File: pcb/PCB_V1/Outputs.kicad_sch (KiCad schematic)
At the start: 18 parts, among them J501 FAN1 / WAGO 2601, J511 FAN2 / WAGO 2601, J521 PUMP + / switched -, Q501 AO3400A, Q511 AO3400A, Q521 AO3400A

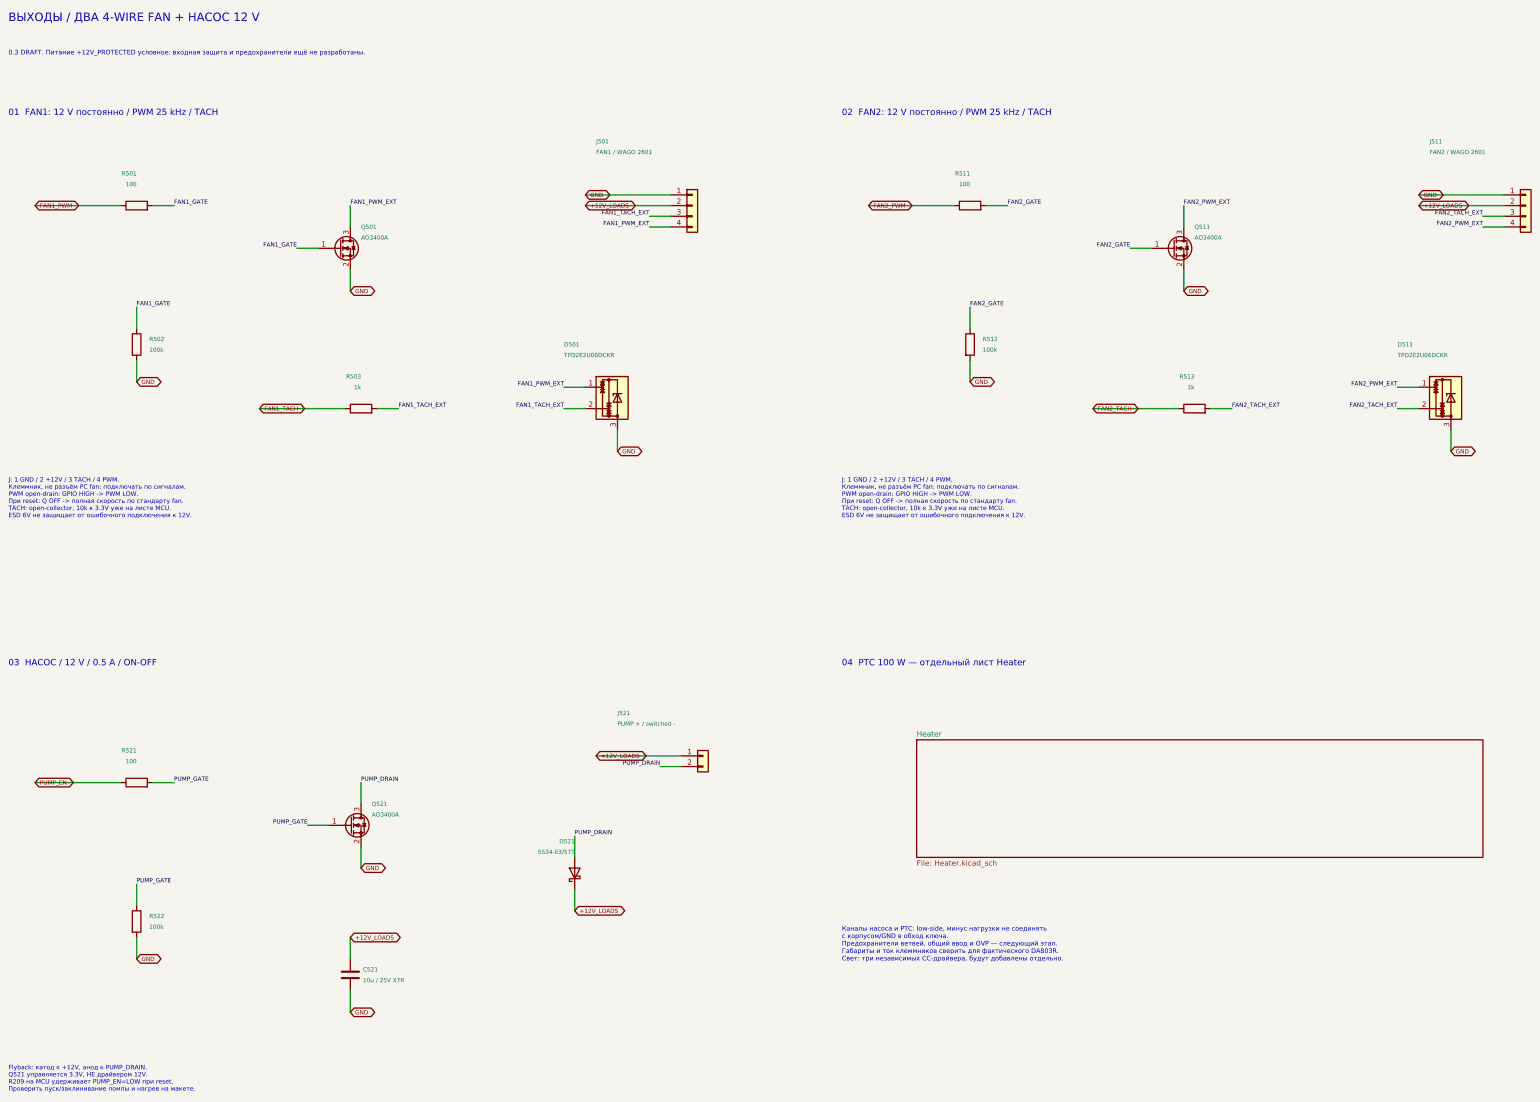
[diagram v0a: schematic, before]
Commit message: pcb: move board to 24 V input with 12 V aux buck and merged LED bar channel
Revision 0.14 of PCB_V1 (see pcb/PCB_V1/REDESIGN_24V.md):
- 24 V input on keyed XT60PW-M (pin 1 GND, pin 2 +24V); LM74700, input
  MOSFET and F901 removed; SMBJ26CA TVS; 220 uF/50 V bulk
- ATM mini-blade fuses in XF-508P-B-B holders: F902 10 A loads, F903 7.5 A LED
- new LMR16020 24 V -> 12 V aux buck (500 kHz) feeding PC fans, the
  UCC27524A heater gate driver and the TPS54202 3.3 V buck; TPS70950 removed
- heater and pump on 24 V: SMBJ30A drain TVS, AO3422 + SS36 pump stage
- LED CH1 panel keeps SRP1770TA/0.027 R/1k, switch now CSD19534Q5A;
  CH2 drives both identical bars in parallel (J721 || J731, 0.40 R);
  third AL8853 channel removed
- TS-1187A buttons, DORABO/KANGNEX terminals
- project library: LMR16020 and CSD19534Q5A symbols, TI DQJ and XF-508P
  footprints
- verify_netlist.py / verify_board.py / analyze_*.py updated for 24 V;
  new sync_board.py updates the unrouted staging board from the netlist
- ERC 0/0; netlist, board and sizing checks pass; DRC only the 12 known
  ESP32 drill sizes plus unrouted connections; 163 components

Co-Authored-By: Claude Opus 5.5 <noreply@anthropic.com>
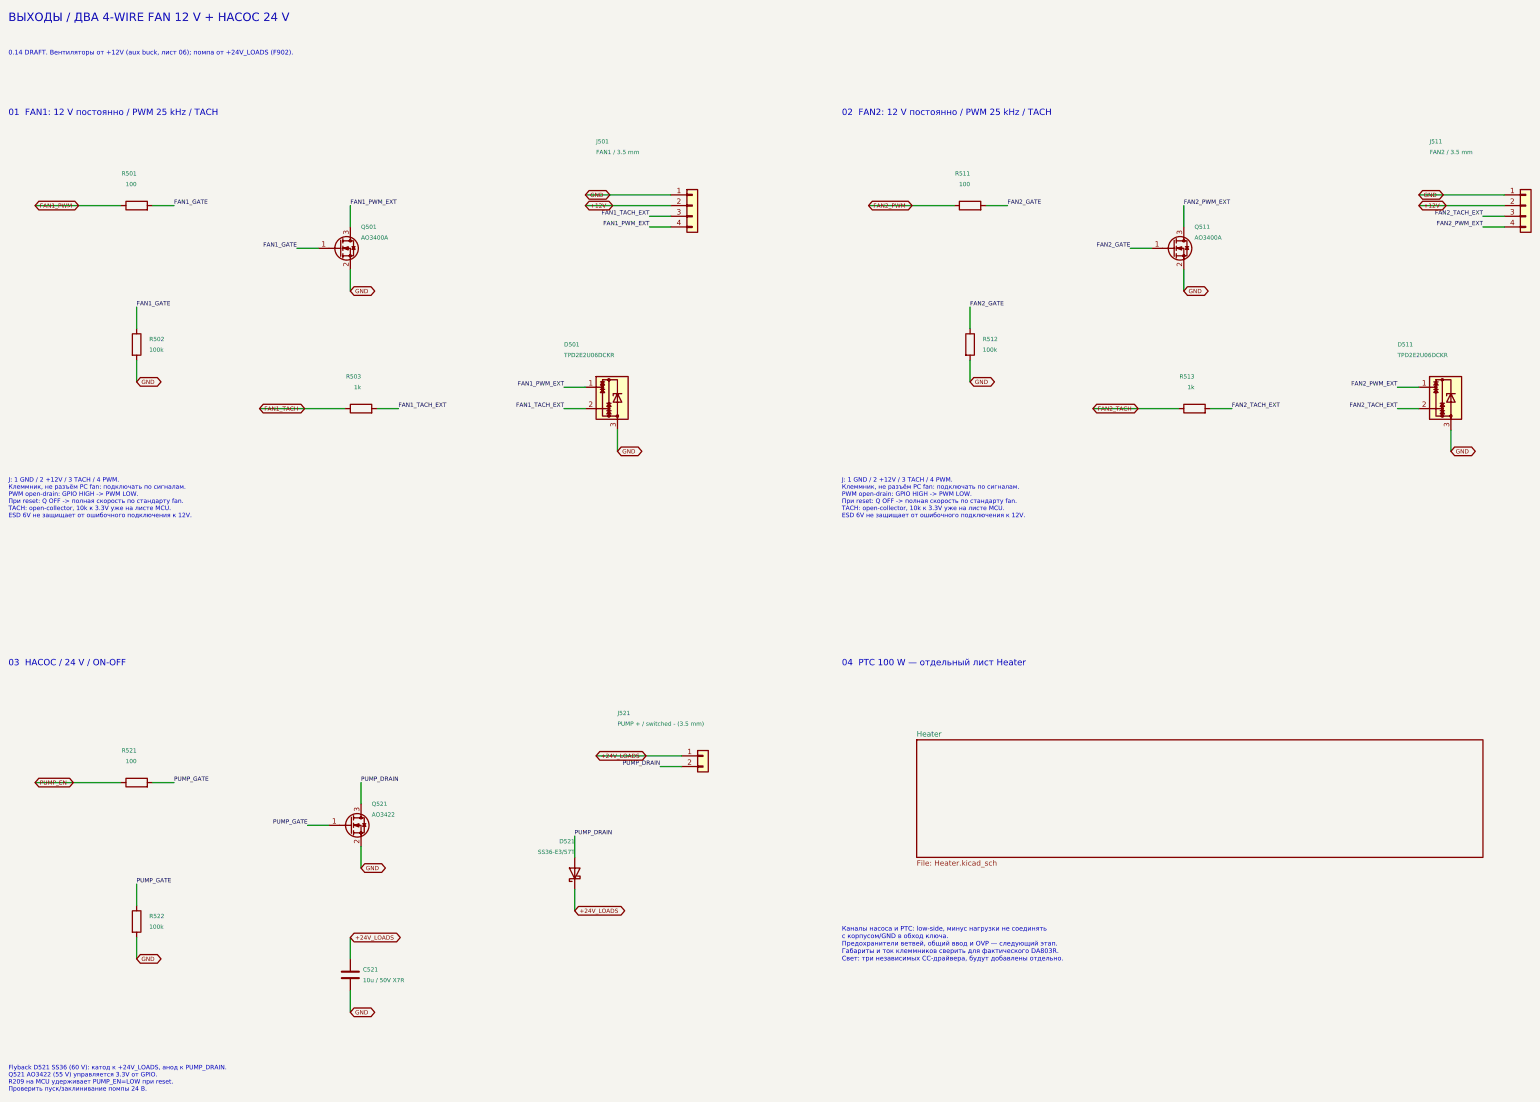
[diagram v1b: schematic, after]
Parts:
- C521: value 10u / 25V X7R -> 10u / 50V X7R; LCSC (none) -> C77102; MPN (none) -> GRM32ER71H106KA12L; Manufacturer (none) -> Murata
- D521: value SS34-E3/57T -> SS36-E3/57T; LCSC (none) -> C35722; MPN (none) -> SS36-E3/57T; Manufacturer (none) -> Vishay
- J501: value FAN1 / WAGO 2601 -> FAN1 / 3.5 mm; footprint TerminalBlock_WAGO:TerminalBlock_WAGO_2601-1104_1x04_P3.50mm_Horizontal -> TerminalBlock_Phoenix:TerminalBlock_Phoenix_PT-1,5-4-3.5-H_1x04_P3.50mm_Horizontal; LCSC (none) -> C2757925; MPN (none) -> DB125-3.5-4P-GN-S; Manufacturer (none) -> DORABO
- J511: value FAN2 / WAGO 2601 -> FAN2 / 3.5 mm; footprint TerminalBlock_WAGO:TerminalBlock_WAGO_2601-1104_1x04_P3.50mm_Horizontal -> TerminalBlock_Phoenix:TerminalBlock_Phoenix_PT-1,5-4-3.5-H_1x04_P3.50mm_Horizontal; LCSC (none) -> C2757925; MPN (none) -> DB125-3.5-4P-GN-S; Manufacturer (none) -> DORABO
- J521: value PUMP + / switched - -> PUMP + / switched - (3.5 mm); footprint TerminalBlock_WAGO:TerminalBlock_WAGO_2601-1102_1x02_P3.50mm_Horizontal -> TerminalBlock_Phoenix:TerminalBlock_Phoenix_PT-1,5-2-3.5-H_1x02_P3.50mm_Horizontal; LCSC (none) -> C466970; MPN (none) -> DB125-3.5-2P-GN-S; Manufacturer (none) -> DORABO
- Q521: value AO3400A -> AO3422; LCSC (none) -> C37130; MPN (none) -> AO3422; Manufacturer (none) -> AOS
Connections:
- net +12V_LOADS renamed +24V_LOADS
- net +24V_LOADS: no longer J501.2 (Pin_2), J511.2 (Pin_2)
- new net +12V: J501.2 (Pin_2), J511.2 (Pin_2)
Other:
- note added: "0.14 DRAFT. Вентиляторы от +12V (aux buck, лист 06); помпа от +24V_LOADS (F902)."
- note added: "03 НАСОС / 24 V / ON-OFF"
- note added: "Flyback D521 SS36 (60 V): катод к +24V_LOADS, анод к PUMP_DRAIN. Q521 AO3422 (55 V) управляется 3.3V от GPIO. R209 на MCU удерживает PUMP_EN=LOW при reset. Проверить пуск/заклинивание помпы 24 В."
- note added: "ВЫХОДЫ / ДВА 4-WIRE FAN 12 V + НАСОС 24 V"
- note removed: "0.3 DRAFT. Питание +12V_PROTECTED условное: входная защита и предохранители ещё не разработаны."
- note removed: "03 НАСОС / 12 V / 0.5 A / ON-OFF"
- note removed: "Flyback: катод к +12V, анод к PUMP_DRAIN. Q521 управляется 3.3V, НЕ драйвером 12V. R209 на MCU удерживает PUMP_EN=LOW при reset. Проверить пуск/заклинивание помпы и нагрев на макете."
- note removed: "ВЫХОДЫ / ДВА 4-WIRE FAN + НАСОС 12 V"
- title: 04 - Fans and pump -> 04 - Fans (12 V aux) and pump (24 V)
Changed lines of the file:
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@@
 	(paper "A3")
 	(title_block
-		(title "04 - Fans and pump")
-		(date "2026-09-26")
-		(rev "0.4-DRAFT")
+		(title "04 - Fans (12 V aux) and pump (24 V)")
+		(date "2026-09-27")
+		(rev "0.14-DRAFT")
 		(company "GrowBox controller")
 		(comment 1 "Draft: input protection and LED drivers pending")
@@
 		)
 	)
-	(text "Flyback: катод к +12V, анод к PUMP_DRAIN.\nQ521 управляется 3.3V, НЕ драйвером 12V.\nR209 на MCU удерживает PUMP_EN=LOW при reset.\nПроверить пуск/заклинивание помпы и нагрев на макете."
+	(text "Flyback D521 SS36 (60 V): катод к +24V_LOADS, анод к PUMP_DRAIN.\nQ521 AO3422 (55 V) управляется 3.3V от GPIO.\nR209 на MCU удерживает PUMP_EN=LOW при reset.\nПроверить пуск/заклинивание помпы 24 В."
 		(exclude_from_sim no)
 		(at 20.32 265.43 0)
@@
 		)
 	)
-	(text "0.3 DRAFT. Питание +12V_PROTECTED условное: входная защита и предохранители ещё не разработаны."
+	(text "0.14 DRAFT. Вентиляторы от +12V (aux buck, лист 06); помпа от +24V_LOADS (F902)."
 		(exclude_from_sim no)
 		(at 20.32 24.13 0)
@@
 		)
 	)
-	(text "03  НАСОС / 12 V / 0.5 A / ON-OFF"
+	(text "03  НАСОС / 24 V / ON-OFF"
 		(exclude_from_sim no)
 		(at 20.32 168.91 0)
@@
 		)
 	)
-	(text "ВЫХОДЫ / ДВА 4-WIRE FAN + НАСОС 12 V"
+	(text "ВЫХОДЫ / ДВА 4-WIRE FAN 12 V + НАСОС 24 V"
 		(exclude_from_sim no)
 		(at 20.32 15.24 0)
@@
 		)
 	)
-	(global_label "+12V_LOADS"
+	(global_label "+12V"
 		(shape bidirectional)
 		(at 355.6 60.96 0)
@@
 		)
 	)
-	(global_label "+12V_LOADS"
+	(global_label "+24V_LOADS"
 		(shape bidirectional)
 		(at 154.94 228.6 0)
@@
 		)
 	)
-	(global_label "+12V_LOADS"
+	(global_label "+12V"
 		(shape bidirectional)
 		(at 157.48 60.96 0)
@@
 		)
 	)
-	(global_label "+12V_LOADS"
+	(global_label "+24V_LOADS"
 		(shape bidirectional)
 		(at 160.02 191.77 0)
@@
 		)
 	)
-	(global_label "+12V_LOADS"
+	(global_label "+24V_LOADS"
 		(shape bidirectional)
 		(at 101.6 234.95 0)
@@
 			)
 		)
-		(property "Value" "SS34-E3/57T"
+		(property "Value" "SS36-E3/57T"
 			(at 154.94 214.63 90)
 			(show_name no)
@@
 					(unit 1)
 				)
+			)
+		)
+		(property "LCSC" "C35722"
+			(at 154.94 219.71 0)
+			(effects
+				(font
+					(size 1 1)
+				)
+				(hide yes)
+				(justify left)
+			)
+		)
+		(property "MPN" "SS36-E3/57T"
+			(at 154.94 219.71 0)
+			(effects
+				(font
+					(size 1 1)
+				)
+				(hide yes)
+				(justify left)
+			)
+		)
+		(property "Manufacturer" "Vishay"
+			(at 154.94 219.71 0)
+			(effects
+				(font
+					(size 1 1)
+				)
+				(hide yes)
+				(justify left)
 			)
 		)
@@
 			)
 		)
-		(property "Value" "FAN1 / WAGO 2601"
+		(property "Value" "FAN1 / 3.5 mm"
 			(at 160.02 48.26 0)
 			(show_name no)
@@
 			)
 		)
-		(property "Footprint" "TerminalBlock_WAGO:TerminalBlock_WAGO_2601-1104_1x04_P3.50mm_Horizontal"
+		(property "Footprint" "TerminalBlock_Phoenix:TerminalBlock_Phoenix_PT-1,5-4-3.5-H_1x04_P3.50mm_Horizontal"
 			(at 182.88 60.96 0)
 			(hide yes)
@@
 					(unit 1)
 				)
+			)
+		)
+		(property "LCSC" "C2757925"
+			(at 182.88 60.96 0)
+			(effects
+				(font
+					(size 1 1)
+				)
+				(hide yes)
+				(justify left)
+			)
+		)
+		(property "MPN" "DB125-3.5-4P-GN-S"
+			(at 182.88 60.96 0)
+			(effects
+				(font
+					(size 1 1)
+				)
+				(hide yes)
+				(justify left)
+			)
+		)
+		(property "Manufacturer" "DORABO"
+			(at 182.88 60.96 0)
+			(effects
+				(font
+					(size 1 1)
+				)
+				(hide yes)
+				(justify left)
 			)
 		)
@@
 			)
 		)
-		(property "Value" "PUMP + / switched -"
+		(property "Value" "PUMP + / switched - (3.5 mm)"
 			(at 165.1 184.15 0)
 			(show_name no)
@@
 			)
 		)
-		(property "Footprint" "TerminalBlock_WAGO:TerminalBlock_WAGO_2601-1102_1x02_P3.50mm_Horizontal"
+		(property "Footprint" "TerminalBlock_Phoenix:TerminalBlock_Phoenix_PT-1,5-2-3.5-H_1x02_P3.50mm_Horizontal"
 			(at 185.42 191.77 0)
 			(hide yes)
@@
 					(unit 1)
 				)
+			)
+		)
+		(property "LCSC" "C466970"
+			(at 185.42 191.77 0)
+			(effects
+				(font
+					(size 1 1)
+				)
+				(hide yes)
+				(justify left)
+			)
+		)
+		(property "MPN" "DB125-3.5-2P-GN-S"
+			(at 185.42 191.77 0)
+			(effects
+				(font
+					(size 1 1)
+				)
+				(hide yes)
+				(justify left)
+			)
+		)
+		(property "Manufacturer" "DORABO"
+			(at 185.42 191.77 0)
+			(effects
+				(font
+					(size 1 1)
+				)
+				(hide yes)
+				(justify left)
 			)
 		)
@@
 			)
 		)
-		(property "Value" "FAN2 / WAGO 2601"
+		(property "Value" "FAN2 / 3.5 mm"
 			(at 358.14 48.26 0)
 			(show_name no)
@@
 			)
 		)
-		(property "Footprint" "TerminalBlock_WAGO:TerminalBlock_WAGO_2601-1104_1x04_P3.50mm_Horizontal"
+		(property "Footprint" "TerminalBlock_Phoenix:TerminalBlock_Phoenix_PT-1,5-4-3.5-H_1x04_P3.50mm_Horizontal"
 			(at 381 60.96 0)
 			(hide yes)
@@
 					(unit 1)
 				)
+			)
+		)
+		(property "LCSC" "C2757925"
+			(at 381 60.96 0)
+			(effects
+				(font
+					(size 1 1)
+				)
+				(hide yes)
+				(justify left)
+			)
+		)
+		(property "MPN" "DB125-3.5-4P-GN-S"
+			(at 381 60.96 0)
+			(effects
+				(font
+					(size 1 1)
+				)
+				(hide yes)
+				(justify left)
+			)
+		)
+		(property "Manufacturer" "DORABO"
+			(at 381 60.96 0)
+			(effects
+				(font
+					(size 1 1)
+				)
+				(hide yes)
+				(justify left)
 			)
 		)
@@
 			)
 		)
-		(property "Value" "10u / 25V X7R"
+		(property "Value" "10u / 50V X7R"
 			(at 104.6 245.11 0)
 			(show_name no)
@@
 					(unit 1)
 				)
+			)
+		)
+		(property "LCSC" "C77102"
+			(at 101.6 243.84 0)
+			(effects
+				(font
+					(size 1 1)
+				)
+				(hide yes)
+				(justify left)
+			)
+		)
+		(property "MPN" "GRM32ER71H106KA12L"
+			(at 101.6 243.84 0)
+			(effects
+				(font
+					(size 1 1)
+				)
+				(hide yes)
+				(justify left)
+			)
+		)
+		(property "Manufacturer" "Murata"
+			(at 101.6 243.84 0)
+			(effects
+				(font
+					(size 1 1)
+				)
+				(hide yes)
+				(justify left)
 			)
 		)
@@
 			)
 		)
-		(property "Value" "AO3400A"
+		(property "Value" "AO3422"
 			(at 106.68 205.74 0)
 			(show_name no)
@@
 			)
 		)
+		(property "LCSC" "C37130"
+			(at 101.6 208.28 0)
+			(effects
+				(font
+					(size 1 1)
+				)
+				(hide yes)
+				(justify left)
+			)
+		)
+		(property "MPN" "AO3422"
+			(at 101.6 208.28 0)
+			(effects
+				(font
+					(size 1 1)
+				)
+				(hide yes)
+				(justify left)
+			)
+		)
+		(property "Manufacturer" "AOS"
+			(at 101.6 208.28 0)
+			(effects
+				(font
+					(size 1 1)
+				)
+				(hide yes)
+				(justify left)
+			)
+		)
